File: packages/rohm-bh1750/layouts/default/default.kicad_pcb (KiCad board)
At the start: 2 copper layers, 6 parts

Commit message: rohm-bh1750: create, rebuild scd40 and bh1750 packages with hide_designators
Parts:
- added R4: 10kΩ ±1% 62.5mW, UNI_ROYAL_0402WGF1002TCE:R0402, F.Cu at (2.50, 1.25)
- R1: value 10kΩ ±1% 62.5mW -> 1kΩ ±1% 62.5mW; footprint UNI_ROYAL_0402WGF1002TCE:R0402 -> UNI_ROYAL_0402WGF1001TCE:R0402
- U1: footprint Analog_Devices_ADXL375BCCZ_RL7:LGA-14_L5.0-W3.0-P0.80-BL -> ROHM_Semicon_BH1750FVI_TR:WSOF-6_L2.6-W1.6-P0.50-TL-EP
- moved C1 7.42 mm to (-3.25, -1.25), turned to 180 degrees
- moved C2 6.37 mm to (3.75, 1.25)
- moved R3 5.15 mm to (2.50, -1.25)
- moved R2 3.76 mm to (-3.00, 0.00), turned to 0 degrees
- moved R1 2.55 mm to (3.75, -1.25), turned to -90 degrees
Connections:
- C1 pad 1: hv -> VCC
- C1 pad 2: -gnd -> gnd
- C2 pad 1: hv -> DVI
- C2 pad 2: -gnd -> gnd
- R1 pad 1: nCS -> VCC
- R1 pad 2: hv -> DVI
- R2 pad 1: SCL_SCLK -> gnd
- R2 pad 2: hv -> ADDR
- R3 pad 1: SDA_SDI_SDIO -> SCL
- R3 pad 2: hv -> VCC
- U1 pad 1: hv -> VCC
- U1 pad 2: -gnd -> ADDR
- U1 pad 3: RESERVED -> gnd
- U1 pad 4: -gnd -> SDA
- U1 pad 5: -gnd -> DVI
- U1 pad 6: hv -> SCL
- U1 pad 7: nCS -> gnd
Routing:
- net hv: track 29.7 -> 0.00 mm
- net -gnd: track 13.0 -> 0.00 mm, vias 1 -> 0
- net VCC: track 0.00 -> 11.7 mm, vias 0 -> 2
- net gnd: track 0.00 -> 7.16 mm, vias 0 -> 2
- net nCS: track 3.98 -> 0.00 mm
- net SCL_SCLK: track 3.98 -> 0.00 mm
- net DVI: track 0.00 -> 3.80 mm
- net SDA_SDI_SDIO: track 1.91 -> 0.00 mm
- net SDA: track 0.00 -> 1.20 mm
- net SCL: track 0.00 -> 1.20 mm
- net ADDR: track 0.00 -> 1.14 mm

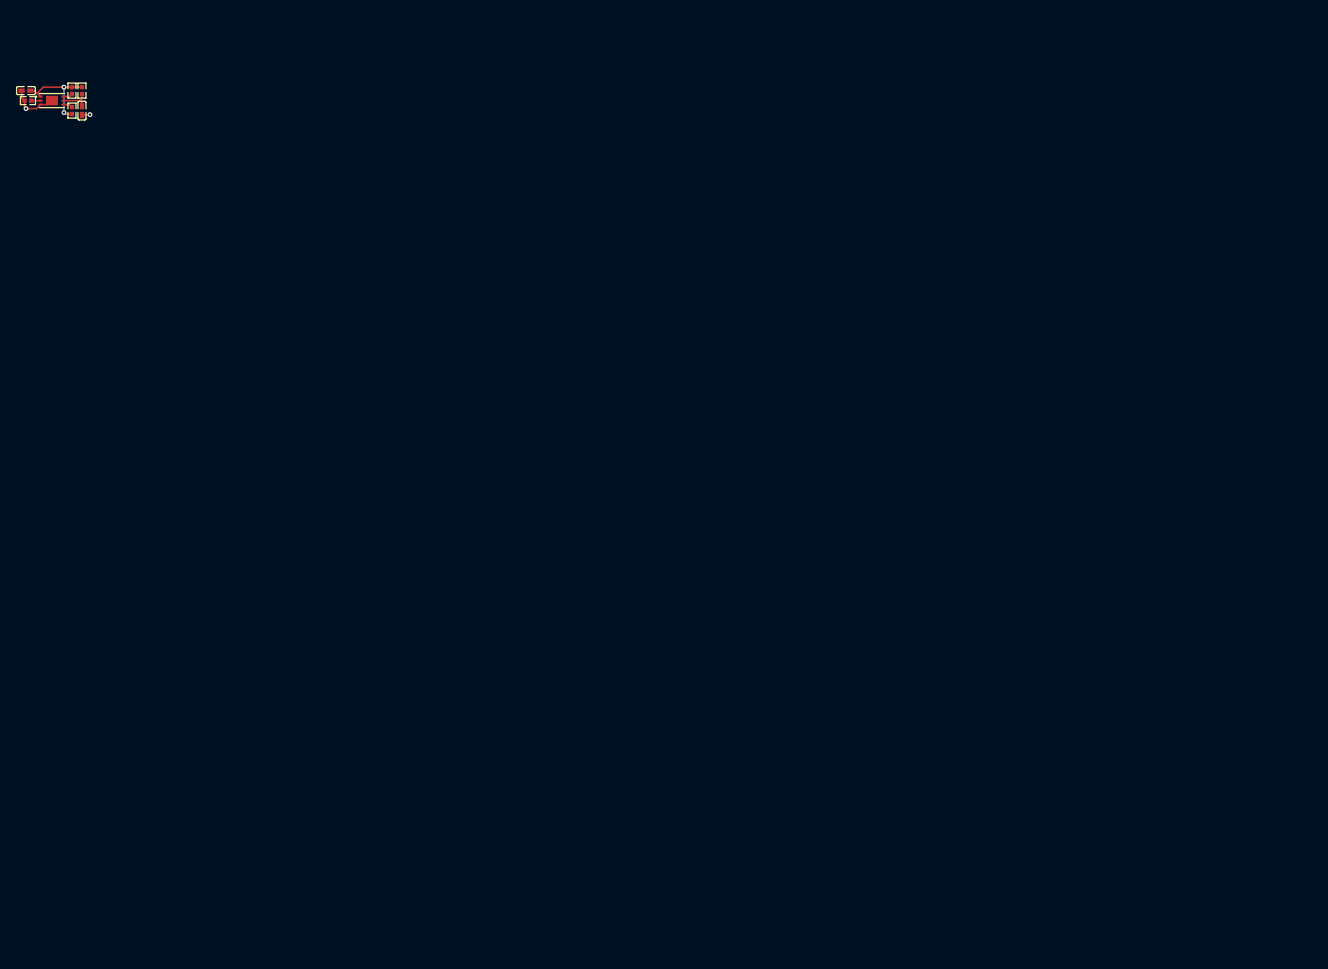
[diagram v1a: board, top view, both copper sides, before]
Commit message: update rohm-bh1750
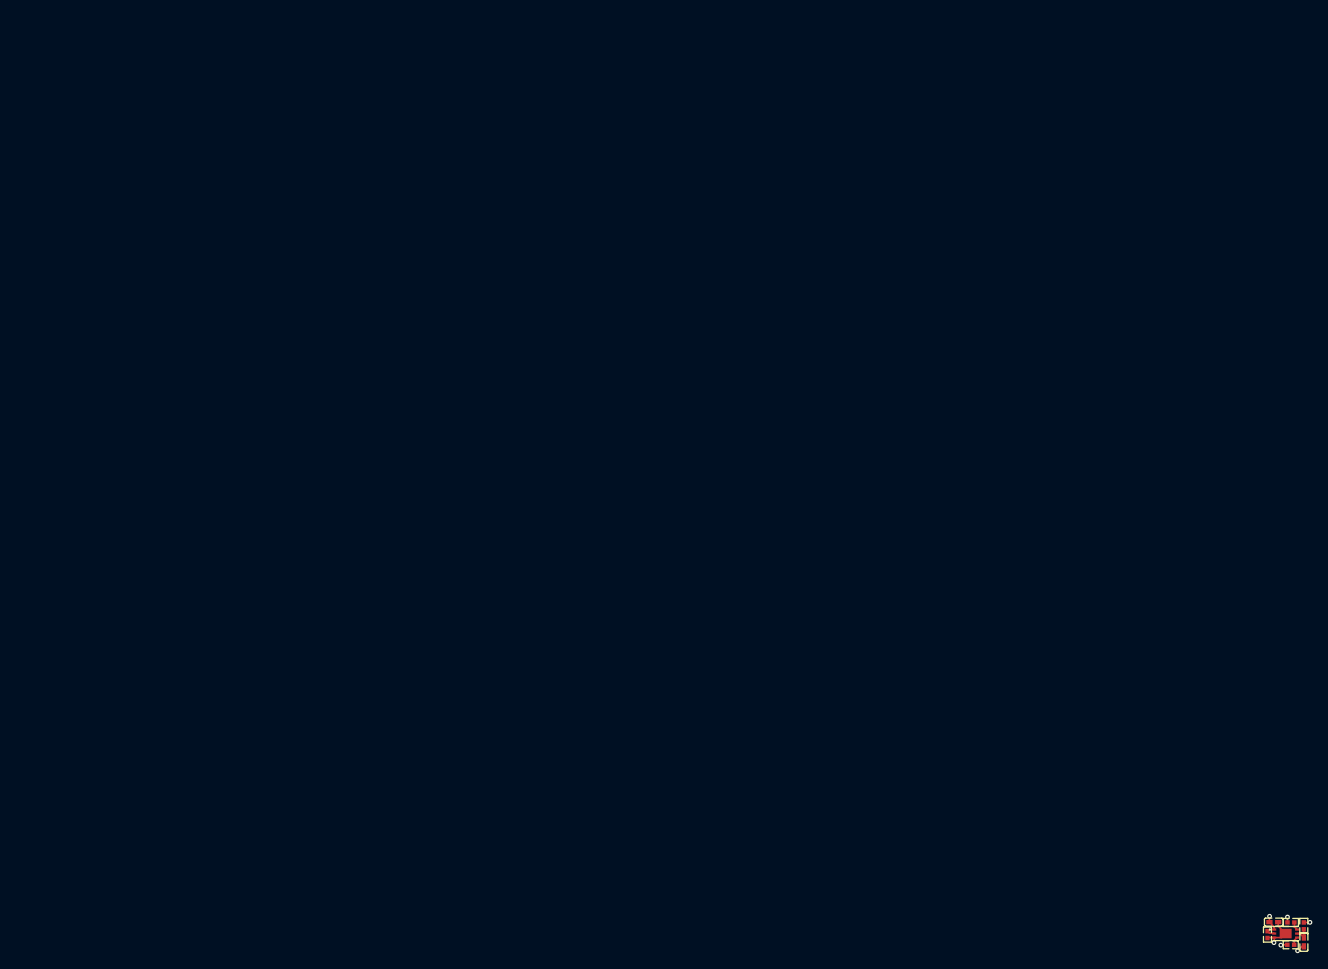
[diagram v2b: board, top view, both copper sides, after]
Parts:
- moved C1 187.4 mm to (152.7, 102.7), turned to 0 degrees
- moved R2 186.7 mm to (151.9, 104.2), turned to 90 degrees
- moved U1 186.1 mm to (154.2, 104.1)
- moved R1 185.0 mm to (156.5, 103.2)
- moved C2 184.7 mm to (156.5, 105.2)
- moved R4 184.6 mm to (154.8, 105.5), turned to 180 degrees
- moved R3 184.5 mm to (154.9, 102.7), turned to 180 degrees
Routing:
- net VCC: track 11.7 -> 4.19 mm, vias 2 -> 4
- net DVI: track 3.80 -> 2.08 mm
- net gnd: track 7.16 -> 5.98 mm

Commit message: Clean PR: Only include packages from package-todos.md
- Updated layouts and parts for packages listed in package-todos.md only
- Includes adi-ad5693r, adi-adbms6822, adi-adbms6830, adi-adxl375, adi-ltc4316
- Updated ams-tsl2591, aosong-aht20, bosch sensors, diodes-inc, espressif
- Updated infineon, invensense, issi, liteon, macroblock, maxim components
- Updated memsic, microchip, rohm, nxp, opsco, st, ti, usb-connectors
- Renamed pjrc-teensy_4_1 to pjrc-teensy-4-1 (hyphen naming convention)
- Updated realtek-rtl8305nb

Removed 64+ packages that were not listed in package-todos.md to keep
PR focused only on packages that are being tracked for review.
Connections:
- net gnd renamed GND
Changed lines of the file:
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@@
     (net 4 "SDA")
     (net 5 "SCL")
-    (net 6 "gnd")
+    (net 6 "GND")
     (footprint "UNI_ROYAL_0402WGF1002TCE:R0402"
         (layer "F.Cu")
@@
             )
         )
-        (property "__atopile_lib_fp_hash__" "314ef801-34ac-5527-e257-4ed1ce397b14"
+        (property "__atopile_lib_fp_hash__" "ac993d00-cd2e-9909-323a-aafc825a9032"
             (at 0 0 0)
             (layer "User.9")
@@
             )
         )
-        (property "__atopile_lib_fp_hash__" "8e38460b-800b-def6-ce01-9e36fad13422"
+        (property "__atopile_lib_fp_hash__" "7c45da14-3bc9-9ff3-ac7d-f87868332dd6"
             (at 0 0 0)
             (layer "User.9")
@@
             (at 0 0 0)
             (layer "User.9")
-            (hide yes)
-            (effects
-                (font
-                    (size 0.125 0.125)
-                    (thickness 0.01875)
-                )
-            )
-        )
-        (property "__atopile_lib_fp_hash__" "04469f6f-d2b4-cef7-91d1-a70362c6f7de"
+            (hide no)
+            (effects
+                (font
+                    (size 0.125 0.125)
+                    (thickness 0.01875)
+                )
+                (hide yes)
+            )
+        )
+        (property "__atopile_lib_fp_hash__" "294059a7-4e3b-089b-5940-774790c8350f"
             (at 0 0 0)
             (layer "User.9")
@@
             (layer "F.Fab")
         )
+        (fp_text user "%R"
+            (at 0 0 0)
+            (layer "F.Fab")
+            (effects
+                (font
+                    (size 1 1)
+                    (thickness 0.15)
+                )
+            )
+            (unlocked no)
+        )
         (fp_text user "${REFERENCE}"
-            (at 0 0 0)
-            (layer "F.Fab")
-            (hide yes)
+            (at 0 -4.5 0)
+            (layer "F.SilkS")
             (effects
                 (font
@@
             (at -1.43 -0.5 0)
             (size 0.51 0.28)
-            (layers "F.Cu" "F.Mask" "F.Paste")
+            (layers "F.Cu" "F.Paste" "F.Mask")
             (net 1 "VCC")
         )
@@
             (at -1.43 0 0)
             (size 0.51 0.28)
-            (layers "F.Cu" "F.Mask" "F.Paste")
+            (layers "F.Cu" "F.Paste" "F.Mask")
             (net 3 "ADDR")
         )
@@
             (at -1.43 0.5 0)
             (size 0.51 0.28)
-            (layers "F.Cu" "F.Mask" "F.Paste")
-            (net 6 "gnd")
+            (layers "F.Cu" "F.Paste" "F.Mask")
+            (net 6 "GND")
         )
         (pad "4" smd rect
             (at 1.43 0.5 0)
             (size 0.51 0.28)
-            (layers "F.Cu" "F.Mask" "F.Paste")
+            (layers "F.Cu" "F.Paste" "F.Mask")
             (net 4 "SDA")
         )
@@
             (at 1.43 0 0)
             (size 0.51 0.28)
-            (layers "F.Cu" "F.Mask" "F.Paste")
+            (layers "F.Cu" "F.Paste" "F.Mask")
             (net 2 "DVI")
         )
@@
             (at 1.43 -0.5 0)
             (size 0.51 0.28)
-            (layers "F.Cu" "F.Mask" "F.Paste")
+            (layers "F.Cu" "F.Paste" "F.Mask")
             (net 5 "SCL")
         )
@@
             (at 0 0 0)
             (size 1.5 1.2)
-            (layers "F.Cu" "F.Mask" "F.Paste")
-            (net 6 "gnd")
-        )
-        (embedded_fonts no)
+            (layers "F.Cu" "F.Paste" "F.Mask")
+            (net 6 "GND")
+        )
         (model "${KIPRJMOD}/../../parts/ROHM_Semicon_BH1750FVI_TR/WSOF-6_L1.6-W2.6-H0.8-P0.50.step"
             (offset
@@
             )
         )
-        (property "__atopile_lib_fp_hash__" "314ef801-34ac-5527-e257-4ed1ce397b14"
+        (property "__atopile_lib_fp_hash__" "ac993d00-cd2e-9909-323a-aafc825a9032"
             (at 0 0 0)
             (layer "User.9")
@@
             )
         )
-        (property "__atopile_lib_fp_hash__" "314ef801-34ac-5527-e257-4ed1ce397b14"
+        (property "__atopile_lib_fp_hash__" "ac993d00-cd2e-9909-323a-aafc825a9032"
             (at 0 0 0)
             (layer "User.9")
@@
             (size 0.57 0.54)
             (layers "F.Cu" "F.Paste" "F.Mask")
-            (net 6 "gnd")
+            (net 6 "GND")
         )
         (model "${KIPRJMOD}/../../parts/UNI_ROYAL_0402WGF1002TCE/R0402_L1.0-W0.5-H0.4.step"
@@
             )
         )
-        (property "__atopile_lib_fp_hash__" "deb0b5cc-bad7-5c07-230d-4a7efb73022f"
+        (property "__atopile_lib_fp_hash__" "f8a97365-7255-729e-24e5-6102db053d76"
             (at 0 0 0)
             (layer "User.9")
@@
             (size 0.79 0.54)
             (layers "F.Cu" "F.Paste" "F.Mask")
-            (net 6 "gnd")
+            (net 6 "GND")
         )
         (pad "1" smd rect
@@
             )
         )
-        (property "__atopile_lib_fp_hash__" "deb0b5cc-bad7-5c07-230d-4a7efb73022f"
+        (property "__atopile_lib_fp_hash__" "f8a97365-7255-729e-24e5-6102db053d76"
             (at 0 0 0)
             (layer "User.9")
@@
             (size 0.79 0.54)
             (layers "F.Cu" "F.Paste" "F.Mask")
-            (net 6 "gnd")
+            (net 6 "GND")
         )
         (pad "1" smd rect

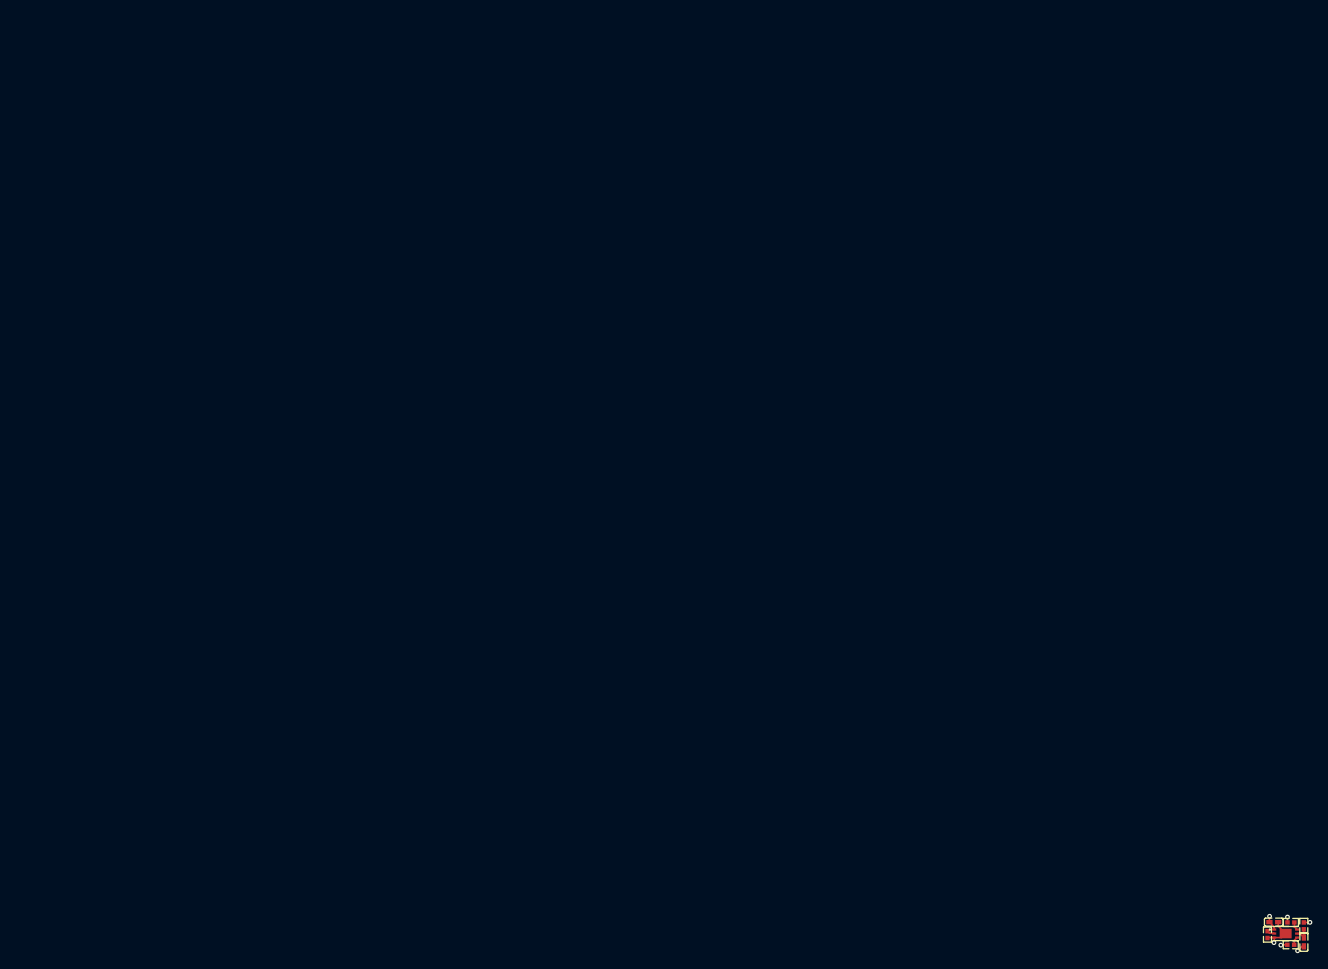
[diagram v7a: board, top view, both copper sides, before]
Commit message: rohm-bh1750: package update to v0.2.0, ato:^0.14.0
Build targets:
  default = rc0
  usage = rc0
Package Verify: rc0
Version: 0.1.3 -> 0.2.0
Requires ato: ^0.14.0
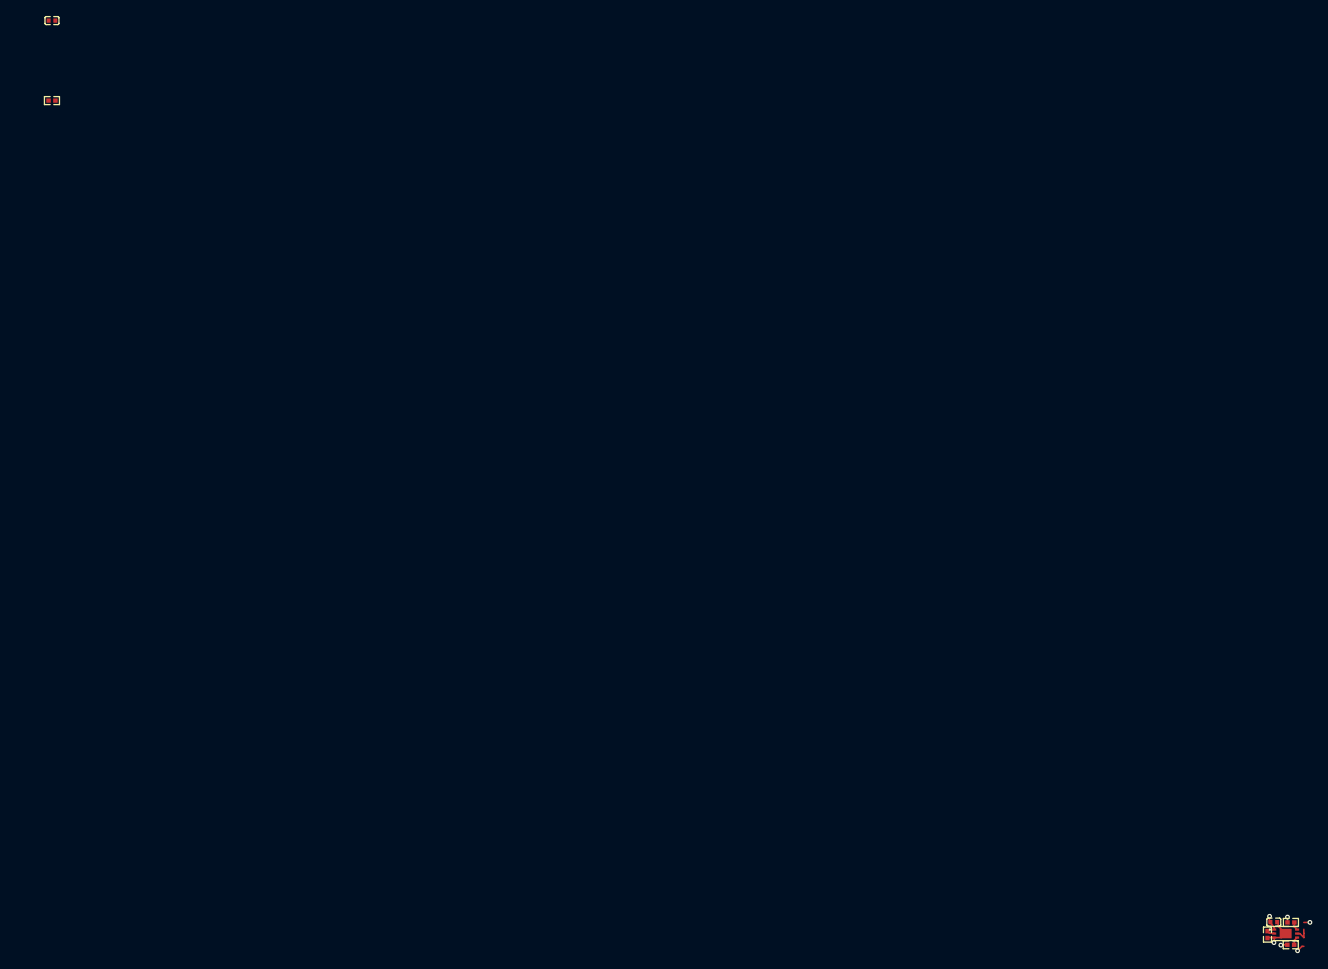
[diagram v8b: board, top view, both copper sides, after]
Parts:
- C1, C2: value 100nF ±10% 16V X7R -> 1±10.0%F
- R1: value 1kΩ ±1% 62.5mW -> 1000±1.0%Ω
- R2, R3, R4: value 10kΩ ±1% 62.5mW -> 10000±1.0%Ω
- moved C2 194.3 mm to (0.00, -10.0), turned to 0 degrees
- moved R1 187.4 mm to (0.00, 0.00), turned to 0 degrees
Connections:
- net DVI renamed dvi_capacitor-power-hv
- net GND renamed lv
- net VCC renamed hv
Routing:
- net lv: track 5.98 -> 0.00 mm, vias 2 -> 0
- net 6: track 0.00 -> 5.98 mm, vias 0 -> 2
- net hv: track 4.19 -> 0.00 mm, vias 4 -> 0
- net 1: track 0.00 -> 4.19 mm, vias 0 -> 4
- net dvi_capacitor-power-hv: track 2.08 -> 0.00 mm
- net 2: track 0.00 -> 2.08 mm
